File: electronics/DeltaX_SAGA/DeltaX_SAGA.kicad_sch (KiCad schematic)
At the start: 62 parts, among them J1 USB_B_Micro, J10 Motor3_Encoder, J11 Motor1_OUT, J12 Motor2_OUT, J13 Motor3_OUT, J2 Programmer, J3 Servo Signal, J4 Servo Power, J5 Power(6-38V), J6 Thrower Signal, J7 Thrower Power, J8 Motor1_Encoder, J9 Motor2_Encoder, U1 CM1223, U10 DRV8243, U11 DRV8243, U2 NCP164C, U3 STM32G441KB, U4 NCV8730, U5 NCP164C, U6 MAX14930, U7 MAX14930, U8 MAX12930, U9 DRV8243

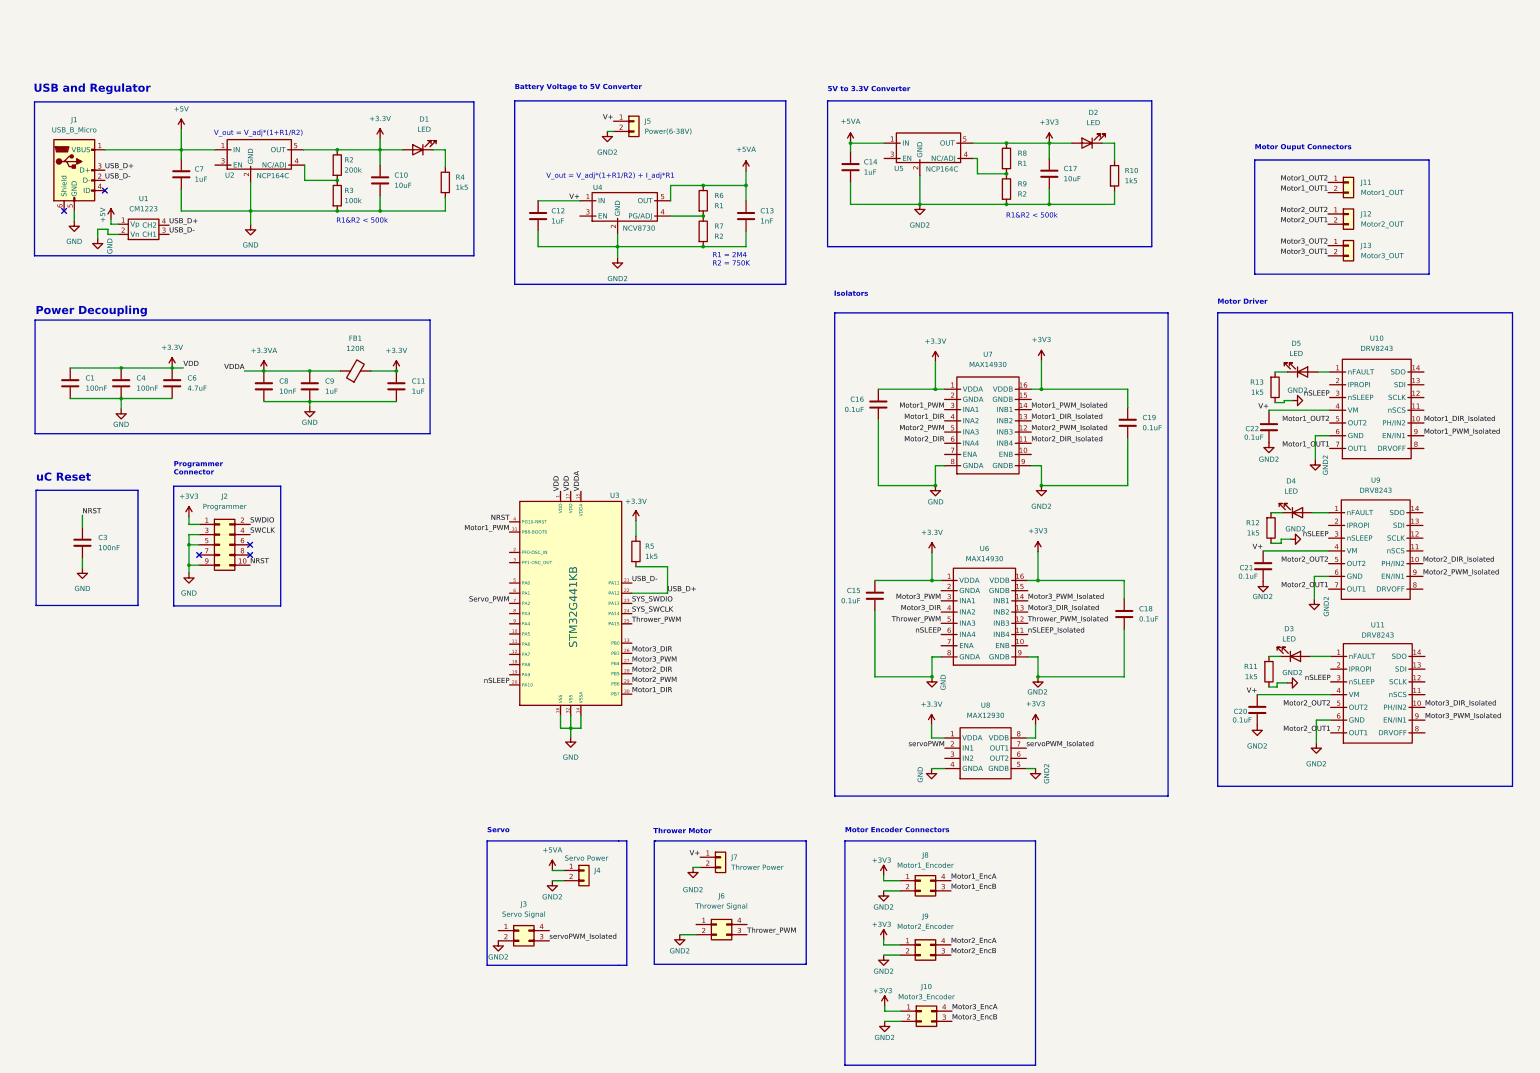
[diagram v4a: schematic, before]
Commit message: Schematic board updated
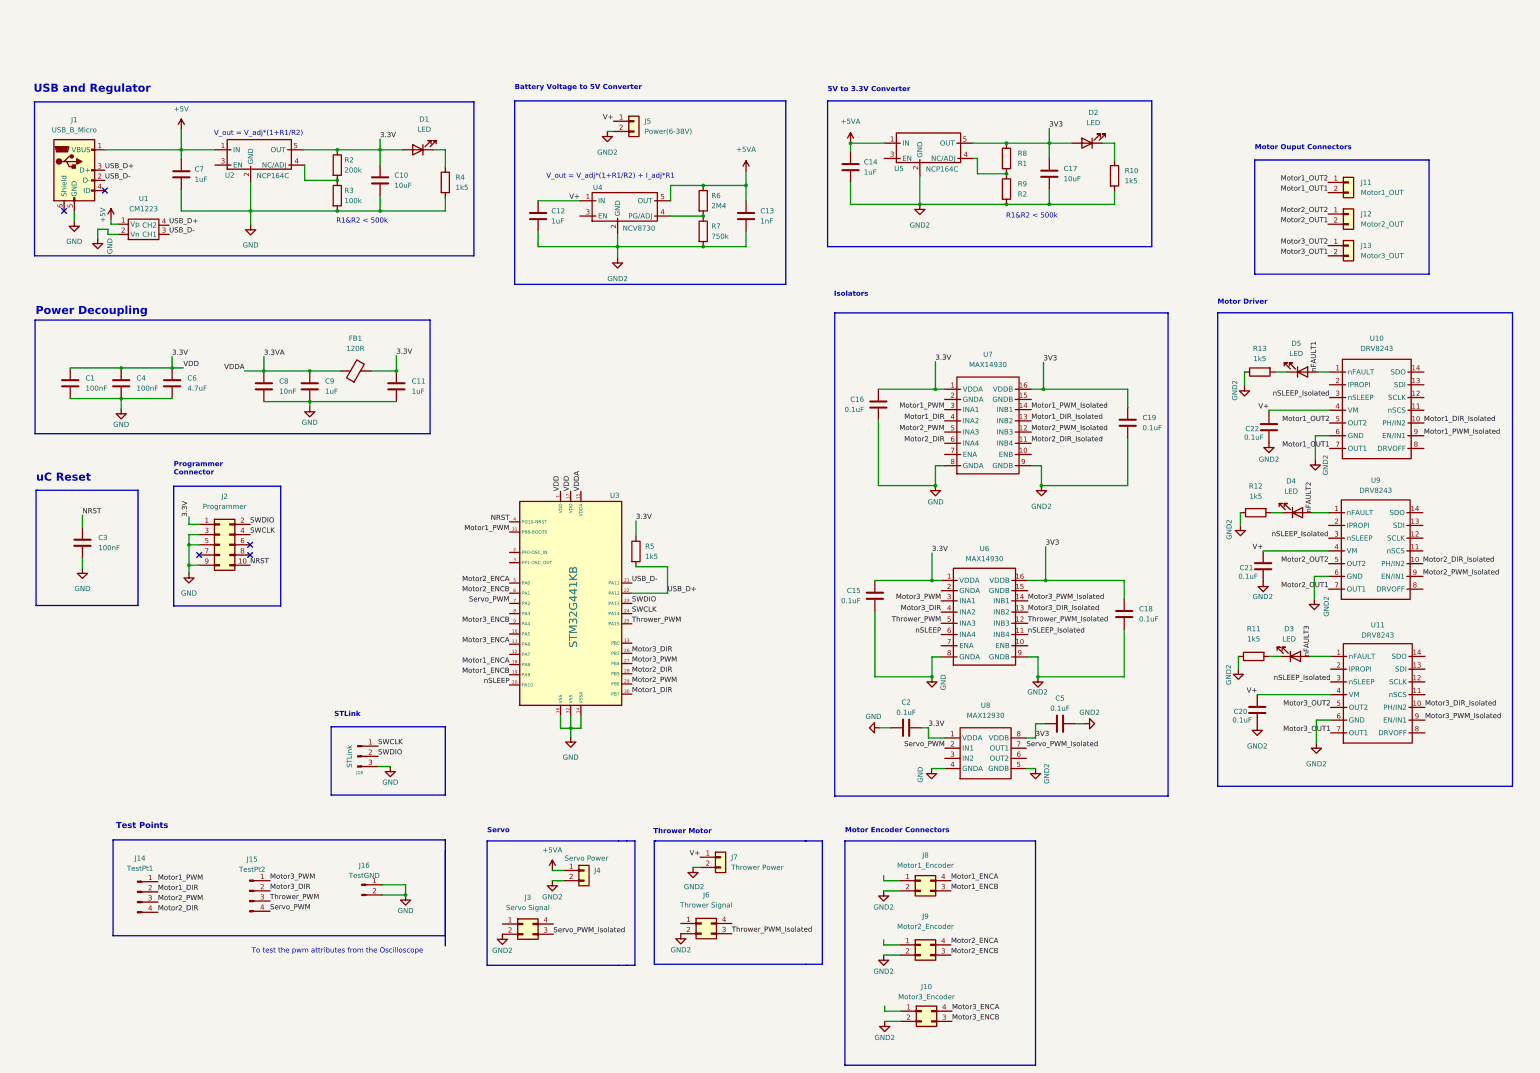
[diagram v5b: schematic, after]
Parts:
- added C2, C5: 0.1uF, Capacitor_SMD:C_0402_1005Metric, symbol Device:C
- added J14: TestPt1, Connector_PinHeader_2.54mm:PinHeader_1x04_P2.54mm_Vertical, symbol Connector:Conn_01x04_Male
- added J15: TestPt2, Connector_PinHeader_2.54mm:PinHeader_1x04_P2.54mm_Vertical, symbol Connector:Conn_01x04_Male
- added J16: TestGND, Connector_PinHeader_2.54mm:PinHeader_1x02_P2.54mm_Vertical, symbol Connector:Conn_01x02_Male
- added J18: STLink, Connector_PinHeader_2.54mm:PinHeader_1x03_P2.54mm_Vertical, symbol Connector:Conn_01x03_Male
- J11, J12, J13, J5, J7: footprint Connector_PinHeader_1.00mm:PinHeader_1x02_P1.00mm_Vertical_SMD_Pin1Right -> Connector_PinHeader_2.54mm:PinHeader_1x02_P2.54mm_Vertical_SMD_Pin1Right
- J4: footprint Connector_PinSocket_2.54mm:PinSocket_1x02_P2.54mm_Vertical_SMD_Pin1Right -> Connector_PinHeader_2.54mm:PinHeader_1x02_P2.54mm_Vertical_SMD_Pin1Right
- R6: value R1 -> 2M4
- R7: value R2 -> 750k
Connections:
- net Motor1_EncA is gone; now on net Motor1_ENCA: J8.4 (Pin_4)
- net Motor1_EncB is gone; now on net Motor1_ENCB: J8.3 (Pin_3)
- net Motor2_EncA is gone; now on net Motor2_ENCA: J9.4 (Pin_4)
- net Motor2_EncB is gone; now on net Motor2_ENCB: J9.3 (Pin_3)
- net Motor3_EncA is gone; now on net Motor3_ENCA: J10.4 (Pin_4)
- net Motor3_EncB is gone; now on net Motor3_ENCB: J10.3 (Pin_3)
- net SYS_SWCLK is gone; now on net SWCLK: U3.24 (PA14)
- net SYS_SWDIO is gone; now on net SWDIO: U3.23 (PA13)
- net servoPWM is gone; now on net Servo_PWM: U8.2 (IN1)
- net GND: now also C2.1, J16.1 (Pin_1), J16.2 (Pin_2), J18.3 (Pin_3)
- net GND2: now also C5.2
- net Motor1_DIR: now also J14.2 (Pin_2)
- net Motor1_PWM: now also J14.1 (Pin_1)
- net Motor2_DIR: now also J14.4 (Pin_4)
- net Motor2_OUT1: no longer U11.7 (OUT1)
- net Motor2_OUT2: no longer U11.5 (OUT2)
- net Motor2_PWM: now also J14.3 (Pin_3)
- net Motor3_DIR: now also J15.2 (Pin_2)
- net Motor3_OUT1: now also U11.7 (OUT1)
- net Motor3_OUT2: now also U11.5 (OUT2)
- net Motor3_PWM: now also J15.1 (Pin_1)
- net SWCLK: now also J18.1 (Pin_1)
- net SWDIO: now also J18.2 (Pin_2)
- net Servo_PWM: now also J15.4 (Pin_4)
- net Thrower_PWM: now also J15.3 (Pin_3); no longer J6.3 (Pin_3)
- net Thrower_PWM_Isolated: now also J6.3 (Pin_3)
- net nSLEEP: no longer U10.3 (nSLEEP), U11.3 (nSLEEP), U9.3 (nSLEEP)
- net nSLEEP_Isolated: now also U10.3 (nSLEEP), U11.3 (nSLEEP), U9.3 (nSLEEP)
- net nFAULT3: now reaches D3.2 (A), U11.1 (nFAULT)
- net 3V3: now reaches R8.1, U5.5 (OUT)
- net 3V3: now also C17.1, C18.2, C19.2, D2.2 (A), U6.16 (VDDB), U7.16 (VDDB), U8.8 (VDDB), C5.1
- net nFAULT2: now reaches D4.2 (A), U9.1 (nFAULT)
- net Motor3_ENCA: now reaches U3.11 (PA6)
- net Motor1_ENCA: now reaches U3.18 (PA8)
- net Motor1_ENCB: now reaches U3.19 (PA9)
- net Motor2_ENCA: now reaches U3.5 (PA0)
- net Motor2_ENCB: now reaches U3.6 (PA1)
- net Motor3_ENCB: now reaches U3.9 (PA4)
- net nFAULT1: now reaches D5.2 (A), U10.1 (nFAULT)
- net +3.3VA renamed 3.3VA
- net +3V3 renamed 3.3V
- net 3.3V: now also C2.2; no longer C17.1, C18.2, C19.2, D2.2 (A), J10.1 (Pin_1), J8.1 (Pin_1), J9.1 (Pin_1), U6.16 (VDDB), U7.16 (VDDB), U8.8 (VDDB)
- net servoPWM_Isolated renamed Servo_PWM_Isolated
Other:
- note added: "STLink"
- note added: "Test Points"
- note added: "To test the pwm attributes from the Oscilloscope"
- note removed: "R1 = 2M4 R2 = 750K"
- moved on the sheet: J3, J6, R11, R12, R13

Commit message: Updated PCB board
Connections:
- net GND2: now also C18.1, U6.9 (GNDB)
- net Motor1_DIR: now also U7.5 (INA3); no longer U7.4 (INA2)
- net Motor1_DIR_Isolated: now also U7.12 (INB3); no longer U7.13 (INB2)
- net Motor1_PWM: now also U7.6 (INA4); no longer U7.3 (INA1)
- net Motor1_PWM_Isolated: now also U7.11 (INB4); no longer U7.14 (INB1)
- net Motor2_DIR: now also U7.3 (INA1); no longer U7.6 (INA4)
- net Motor2_DIR_Isolated: now also U7.14 (INB1); no longer U7.11 (INB4)
- net Motor2_PWM: now also U7.4 (INA2); no longer U7.5 (INA3)
- net Motor2_PWM_Isolated: now also U7.13 (INB2); no longer U7.12 (INB3)
- net Motor3_DIR: now also U6.5 (INA3); no longer U6.4 (INA2)
- net Motor3_DIR_Isolated: now also U6.12 (INB3); no longer U6.13 (INB2)
- net Motor3_PWM: now also U6.6 (INA4); no longer U6.3 (INA1)
- net Motor3_PWM_Isolated: now also U6.11 (INB4); no longer U6.14 (INB1)
- net Thrower_PWM: now also U6.4 (INA2); no longer U6.5 (INA3)
- net Thrower_PWM_Isolated: now also U6.13 (INB2); no longer U6.12 (INB3)
- net nSLEEP: now also U6.3 (INA1); no longer U6.6 (INA4)
- net nSLEEP_Isolated: now also U6.14 (INB1); no longer U6.11 (INB4)
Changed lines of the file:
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@@
   (junction (at 67.945 153.035) (diameter 0) (color 0 0 0 0)
   )
+  (junction (at 300.99 180.8226) (diameter 0) (color 0 0 0 0)
+  )
   (junction (at 63.754 103.886) (diameter 0) (color 0 0 0 0)
-  )
-  (junction (at 279.5016 180.8734) (diameter 0) (color 0 0 0 0)
   )
   (junction (at 119.634 104.648) (diameter 0) (color 0 0 0 0)
@@
     (stroke (width 0) (type default) (color 0 0 0 0))
   )
+  (wire (pts (xy 302.26 180.8226) (xy 302.26 181.3306))
+    (stroke (width 0) (type default) (color 0 0 0 0))
+  )
   (wire (pts (xy 280.3652 133.1976) (xy 301.8536 133.1976))
     (stroke (width 0) (type default) (color 0 0 0 0))
@@
     (stroke (width 0) (type default) (color 0 0 0 0))
   )
-  (wire (pts (xy 300.99 169.0116) (xy 300.99 180.848))
+  (wire (pts (xy 300.99 169.0116) (xy 300.99 180.8226))
     (stroke (width 0) (type default) (color 0 0 0 0))
   )
@@
     (stroke (width 0) (type default) (color 0 0 0 0))
   )
+  (wire (pts (xy 300.99 180.8226) (xy 300.99 180.848))
+    (stroke (width 0) (type default) (color 0 0 0 0))
+  )
   (wire (pts (xy 163.068 193.675) (xy 165.608 193.675))
     (stroke (width 0) (type default) (color 0 0 0 0))
@@
   )
   (wire (pts (xy 241.046 231.648) (xy 245.11 231.648))
+    (stroke (width 0) (type default) (color 0 0 0 0))
+  )
+  (wire (pts (xy 300.99 180.8226) (xy 302.26 180.8226))
     (stroke (width 0) (type default) (color 0 0 0 0))
   )
@@
     (effects (font (size 1.27 1.27) (thickness 0.254) bold) (justify left bottom))
   )
-  (label "Motor1_PWM" (at 256.2352 114.2746 180)
+  (label "Motor1_PWM" (at 256.2352 122.6566 180)
     (effects (font (size 1.27 1.27)) (justify right bottom))
   )
@@
     (effects (font (size 1.27 1.27)) (justify left bottom))
   )
-  (label "Motor1_DIR" (at 256.2352 117.0686 180)
+  (label "Motor1_DIR" (at 256.2352 119.8626 180)
     (effects (font (size 1.27 1.27)) (justify right bottom))
   )
@@
     (effects (font (size 1.27 1.27)) (justify left bottom))
   )
-  (label "Motor3_DIR_Isolated" (at 276.9616 164.719 0)
+  (label "Motor3_DIR_Isolated" (at 276.9616 167.513 0)
     (effects (font (size 1.27 1.27)) (justify left bottom))
   )
@@
     (effects (font (size 1.27 1.27)) (justify right bottom))
   )
-  (label "Thrower_PWM" (at 255.3716 167.513 180)
+  (label "Thrower_PWM" (at 255.3716 164.719 180)
     (effects (font (size 1.27 1.27)) (justify right bottom))
   )
@@
     (effects (font (size 1.27 1.27)) (justify left bottom))
   )
-  (label "nSLEEP" (at 255.3716 170.307 180)
+  (label "nSLEEP" (at 255.3716 161.925 180)
     (effects (font (size 1.27 1.27)) (justify right bottom))
   )
@@
     (effects (font (size 1.27 1.27)) (justify left bottom))
   )
-  (label "Motor2_PWM" (at 256.2352 119.8626 180)
-    (effects (font (size 1.27 1.27)) (justify right bottom))
-  )
-  (label "Motor2_DIR_Isolated" (at 277.8252 122.6566 0)
+  (label "Motor2_PWM" (at 256.2352 117.0686 180)
+    (effects (font (size 1.27 1.27)) (justify right bottom))
+  )
+  (label "Motor2_DIR_Isolated" (at 277.8252 114.2746 0)
     (effects (font (size 1.27 1.27)) (justify left bottom))
   )
@@
     (effects (font (size 1.27 1.27)) (justify left bottom))
   )
-  (label "Motor3_DIR" (at 255.3716 164.719 180)
+  (label "Motor3_DIR" (at 255.3716 167.513 180)
     (effects (font (size 1.27 1.27)) (justify right bottom))
   )
@@
     (effects (font (size 1.27 1.27)) (justify left bottom))
   )
-  (label "Thrower_PWM_Isolated" (at 276.9616 167.513 0)
+  (label "Thrower_PWM_Isolated" (at 276.9616 164.719 0)
     (effects (font (size 1.27 1.27)) (justify left bottom))
   )
@@
     (effects (font (size 1.27 1.27)) (justify left bottom))
   )
-  (label "Motor1_DIR_Isolated" (at 277.8252 117.0686 0)
+  (label "Motor1_DIR_Isolated" (at 277.8252 119.8626 0)
     (effects (font (size 1.27 1.27)) (justify left bottom))
   )
@@
     (effects (font (size 1.27 1.27)) (justify left bottom))
   )
-  (label "Motor2_PWM_Isolated" (at 277.8252 119.8626 0)
+  (label "Motor2_PWM_Isolated" (at 277.8252 117.0686 0)
     (effects (font (size 1.27 1.27)) (justify left bottom))
   )
@@
     (effects (font (size 1.27 1.27)) (justify left bottom))
   )
-  (label "nSLEEP_Isolated" (at 276.9616 170.307 0)
+  (label "nSLEEP_Isolated" (at 276.9616 161.925 0)
     (effects (font (size 1.27 1.27)) (justify left bottom))
   )
@@
     (effects (font (size 1.27 1.27)) (justify left bottom))
   )
-  (label "Motor1_PWM_Isolated" (at 277.8252 114.2746 0)
+  (label "Motor1_PWM_Isolated" (at 277.8252 122.6566 0)
     (effects (font (size 1.27 1.27)) (justify left bottom))
   )
@@
     (effects (font (size 1.27 1.27)) (justify left bottom))
   )
-  (label "Motor3_PWM_Isolated" (at 276.9616 161.925 0)
+  (label "Motor3_PWM_Isolated" (at 276.9616 170.307 0)
     (effects (font (size 1.27 1.27)) (justify left bottom))
   )
@@
     (effects (font (size 1.27 1.27)) (justify left bottom))
   )
-  (label "Motor3_PWM" (at 255.3716 161.925 180)
+  (label "Motor3_PWM" (at 255.3716 170.307 180)
     (effects (font (size 1.27 1.27)) (justify right bottom))
   )
@@
     (effects (font (size 1.27 1.27)) (justify right bottom))
   )
-  (label "Motor2_DIR" (at 256.2352 122.6566 180)
+  (label "Motor2_DIR" (at 256.2352 114.2746 180)
     (effects (font (size 1.27 1.27)) (justify right bottom))
   )
@@
     (pin "1")
   )
-  (symbol (lib_id "power:GND2") (at 279.5016 180.8734 0) (unit 1)
-    (in_bom yes) (on_board yes)
-    (property "Reference" "#PWR041" (id 0) (at 279.5016 187.2234 0)
-      (effects (font (size 1.27 1.27)) hide)
-    )
-    (property "Value" "GND2" (id 1) (at 279.4 184.658 0))
-    (property "Footprint" "" (id 2) (at 279.5016 180.8734 0)
-      (effects (font (size 1.27 1.27)) hide)
-    )
-    (property "Datasheet" "" (id 3) (at 279.5016 180.8734 0)
-      (effects (font (size 1.27 1.27)) hide)
-    )
+  (symbol (lib_id "power:GND2") (at 302.26 181.3306 0) (unit 1)
+    (in_bom yes) (on_board yes)
+    (property "Reference" "#PWR041" (id 0) (at 302.26 187.6806 0)
+      (effects (font (size 1.27 1.27)) hide)
+    )
+    (property "Value" "GND2" (id 1) (at 302.1584 185.1152 0))
+    (property "Footprint" "" (id 2) (at 302.26 181.3306 0)
+      (effects (font (size 1.27 1.27)) hide)
+    )
+    (property "Datasheet" "" (id 3) (at 302.26 181.3306 0)
+      (effects (font (size 1.27 1.27)) hide)
+    )
